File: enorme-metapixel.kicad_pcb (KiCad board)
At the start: 2 copper layers, 75 x 75 mm, 61 parts, among them J1 VIN, J2 STRIP_0, J3 STRIP_1, J4 STRIP_2, J5 UART, J6 VIN, Q1 SSM3K329R, Q2 SSM3K329R, Q3 SSM3K329R, Q4 SSM3K329R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

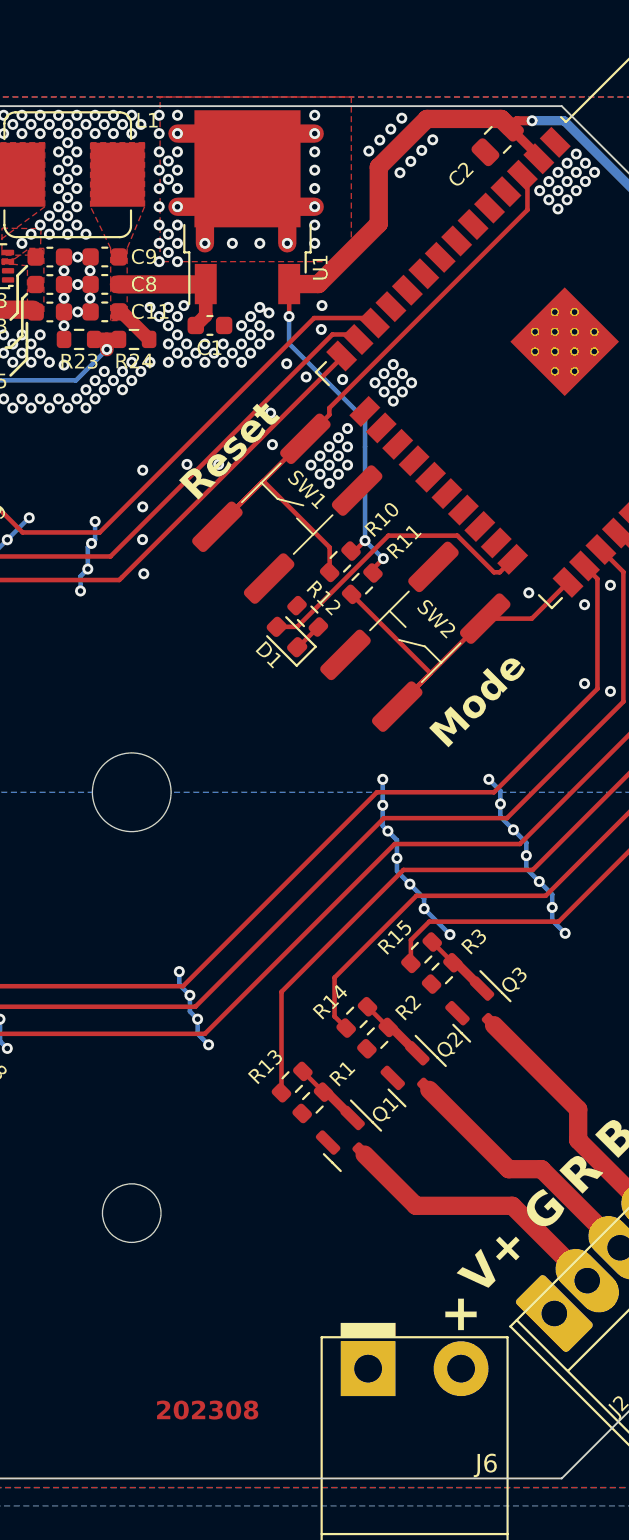
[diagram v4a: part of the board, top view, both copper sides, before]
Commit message: Fix comp refs, replace LDO with easier one easier to get
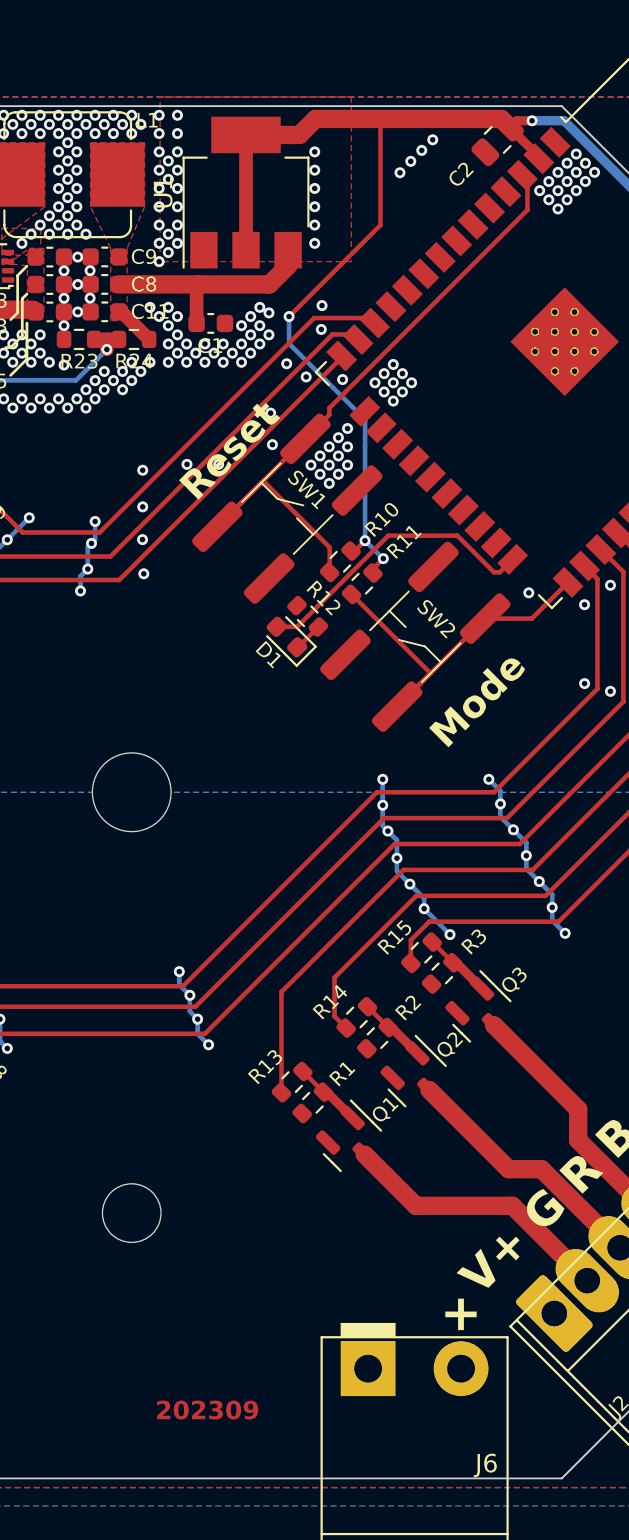
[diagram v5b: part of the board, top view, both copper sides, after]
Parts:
- R1, R2, R3, R4, R5, R6, R7, R8, R9: value 100k -> 100K
- R10, R11: value 10k -> 10K
- R13, R14, R15, R16, R17, R18, R19, R20, R21: value 1k -> 1K
- U1: value BD33FC0FP -> LDL1117-3.3; footprint Package_TO_SOT_SMD:TO-252-2 -> Package_TO_SOT_SMD:SOT-223-3_TabPin2
- moved kibuzzard-63B86E3D 73.0 mm to (115.5, 135.3), turned to 180 degrees
- moved U1 0.80 mm to (106.2, 67.2)
- moved C1 0.12 mm to (104.3, 74.4)
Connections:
- U1 pad 1: +5V -> GND
- U1 pad 2: GND -> +3.3V
- U1 pad 3: +3.3V -> +5V
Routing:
- net GND: track 92.9 -> 62.0 mm, vias 332 -> 320
- net +3.3V: track 81.5 -> 96.1 mm
- net +5V: track 9.52 -> 15.0 mm
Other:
- board text added: "202309"
- board text added: "MetaPixel Rev5"
- board text removed: "202308"
- board text removed: "MetaPixel Rev4"
